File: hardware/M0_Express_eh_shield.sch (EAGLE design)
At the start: 35 parts, among them U1 TLV3691, U2 AB0815, U3 Value, U4 MIC841, U5 TPS781, U6 ISL21080, X2 ABS05-32.768KHZ-9-T

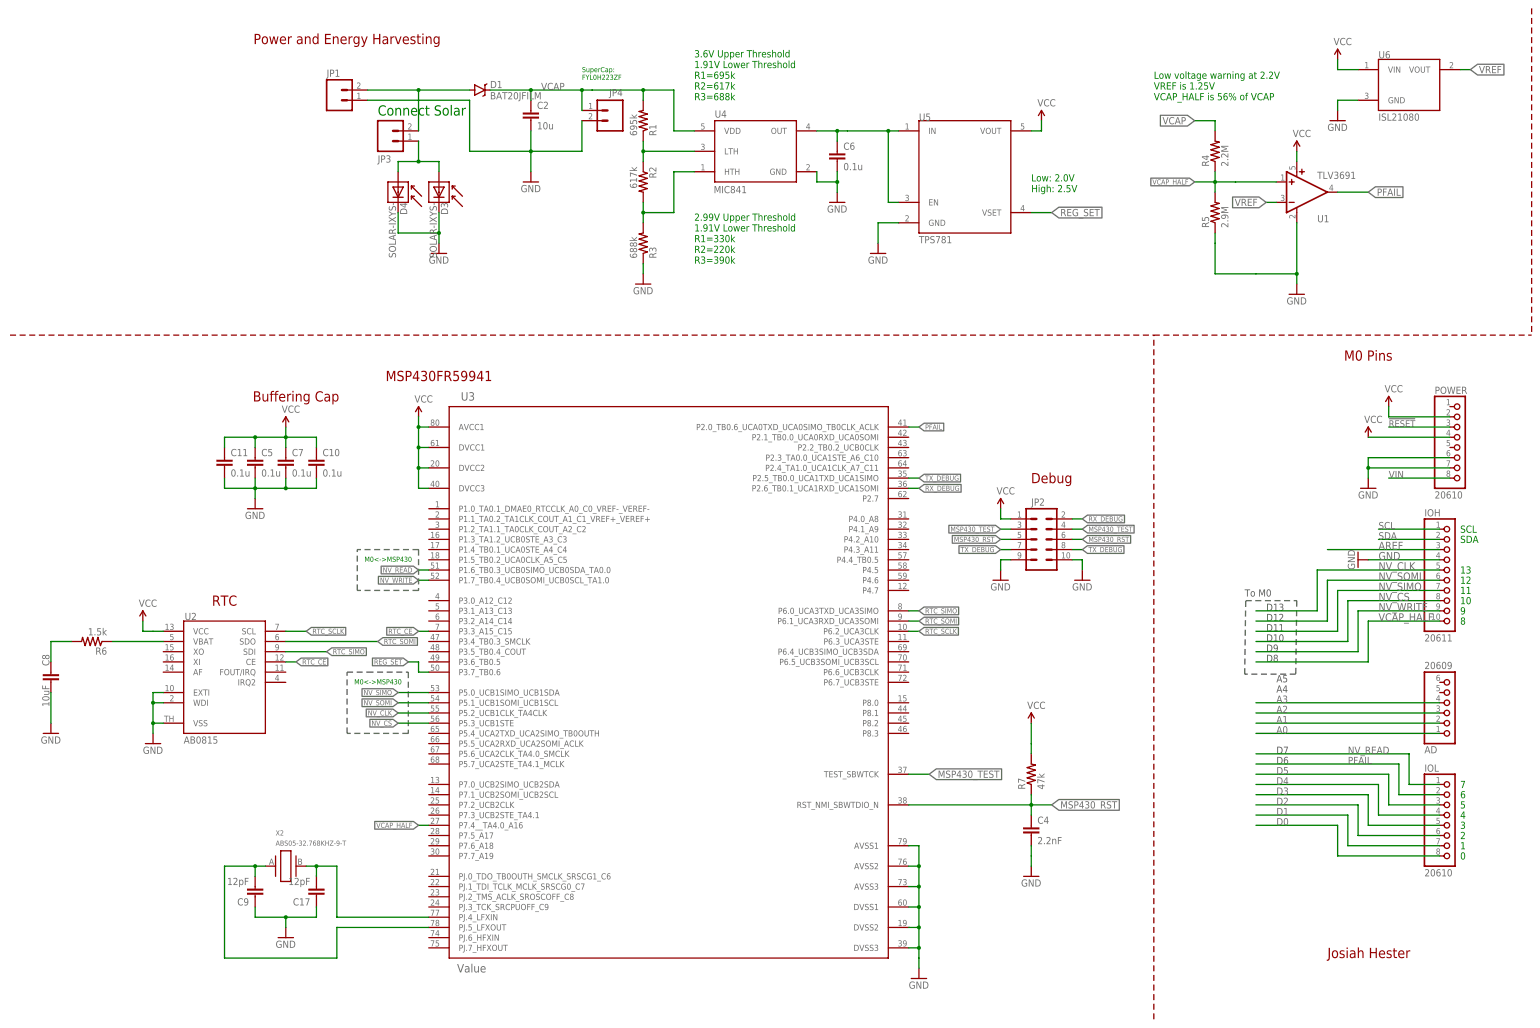
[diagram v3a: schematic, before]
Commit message: updated with parts and final silk
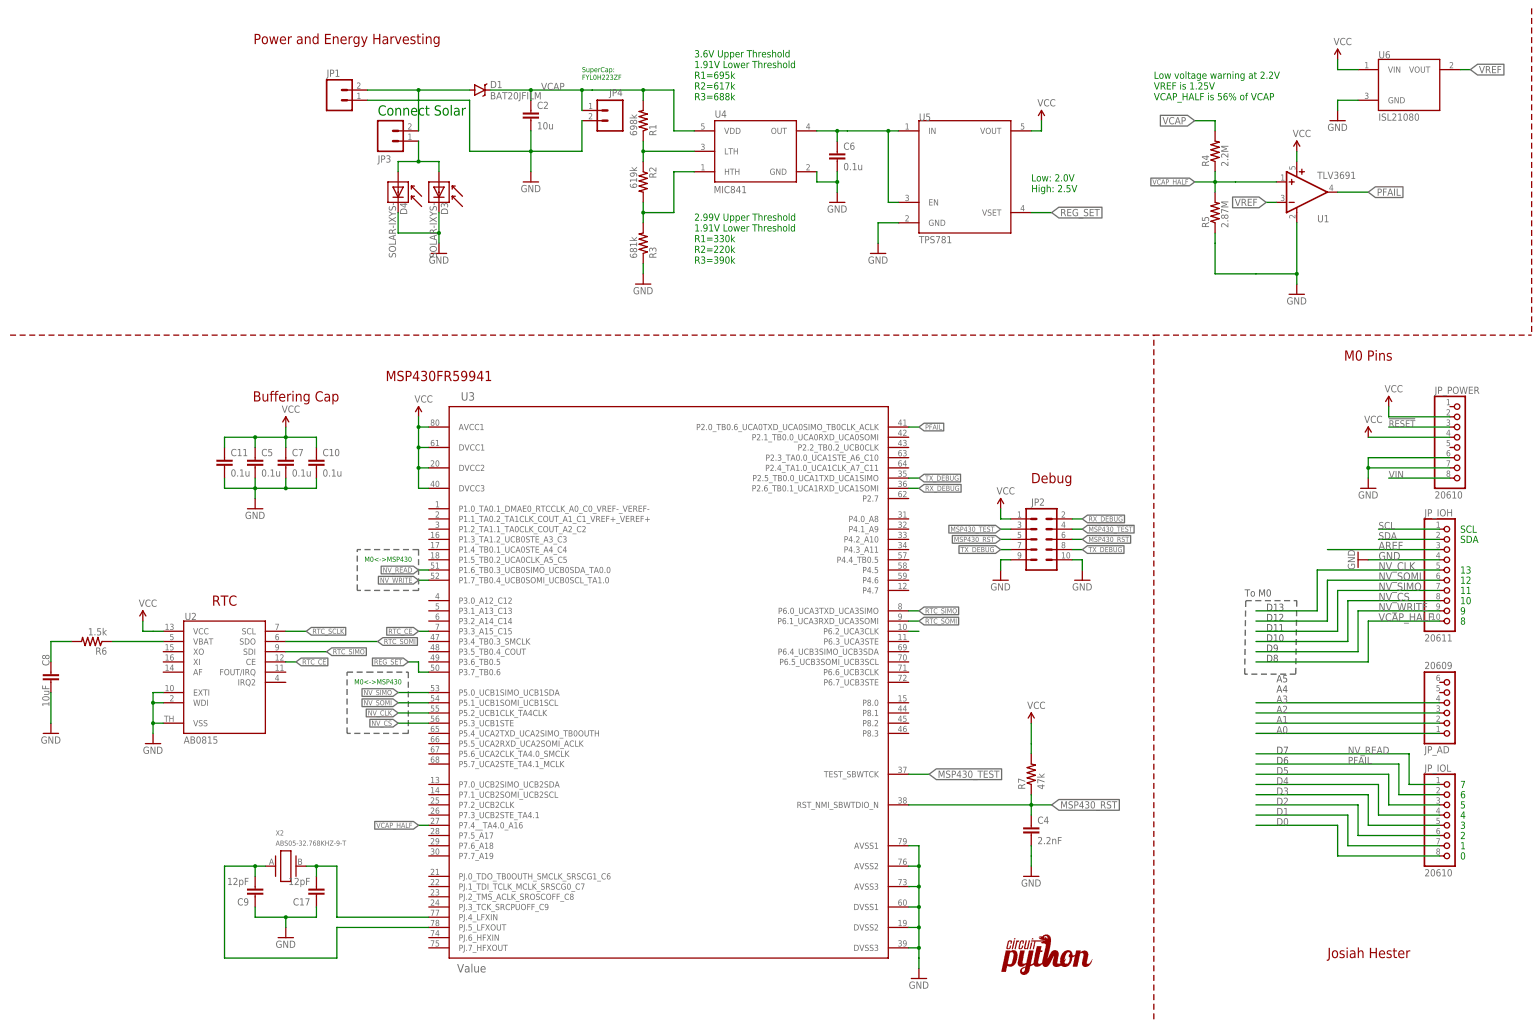
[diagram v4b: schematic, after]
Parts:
- added U$1: LOGO, circuitpython-logo:LOGO
- C10, C11, C5, C6, C7: DIGIKEY (none) -> 1276-1005-1-ND; MPN 06035C222KAT2A -> CL10B104KO8NNNC
- C17, C9: DIGIKEY (none) -> 1276-1254-1-ND
- C2: DIGIKEY (none) -> 1276-6456-1-ND
- C4: DIGIKEY (none) -> 478-1219-1-ND
- C8: DIGIKEY (none) -> 1276-6456-1-ND; MPN 0805YD106KAT2A -> (none)
- D1: DIGIKEY (none) -> NSR0530HT1GOSCT-ND
- D3, D4: MPN (none) -> KXOB25-02X8F
- JP2: MPN (none) -> 3220-10-0100-00
- R1: value 695k -> 698k; DIGIKEY 311-316KHRCT-ND -> 311-698KHRCT-ND; MANUFACTURERPARTNUMBER RC0603FR-07316KL -> (none); MPN RC0603FR-07316KL -> RC0603FR-07698KL
- R2: value 617k -> 619k; DIGIKEY 311-191KHRCT-ND -> 311-619KHRCT-ND; MANUFACTURERPARTNUMBER RC0603FR-07191KL -> (none); MPN RC0603FR-07191KL -> RC0603FR-07619KL
- R3: value 688k -> 681k; DIGIKEY 311-499KHRCT-ND -> RMCF0603FT681KCT-ND; MANUFACTURERPARTNUMBER RC0603FR-07499KL -> (none); MPN RC0603FR-07499KL -> RMCF0603FT681K
- R4: DIGIKEY (none) -> YAG3329CT-ND; MPN (none) -> RC0603FR-072M2L
- R5: value 2.9M -> 2.87M; DIGIKEY (none) -> RMCF0603FT2M87CT-ND; MPN (none) -> RMCF0603FT2M87
- R6: DIGIKEY (none) -> A121524CT-ND; MPN CRCW060347K0JNEA -> CRG0603F1K5
- R7: DIGIKEY (none) -> 541-4061-1-ND; MPN CRCW060347K0JNEA -> CRCW060347K0JNEAC
- U1: DIGIKEY (none) -> 296-37910-1-ND; MPN (none) -> TLV3691IDCKR
- U6: MPN (none) -> ISL21080DIH312Z-TK
- renumbered AD to JP_AD, IOH to JP_IOH, IOL to JP_IOL, POWER to JP_POWER
